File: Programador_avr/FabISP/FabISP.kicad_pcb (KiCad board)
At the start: 2 copper layers, 31.5 x 59.5 mm, 14 parts, among them IC1 ATTINY44-SSU, M1 RESONATOR, M2 PINHD-1x02-SMD-HEADER, M3 MICRO-USB_1_64

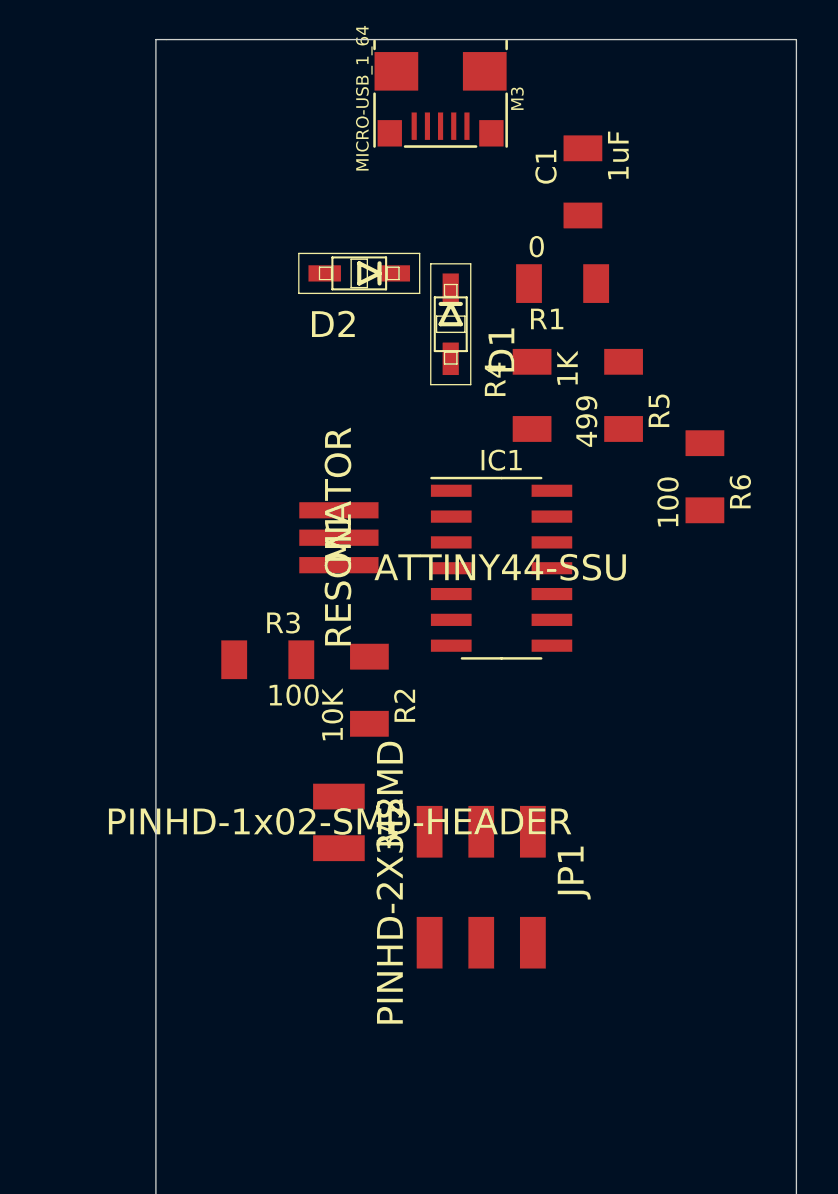
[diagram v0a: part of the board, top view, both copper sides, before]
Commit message: corrección de huellas y primeras rutas de pcb
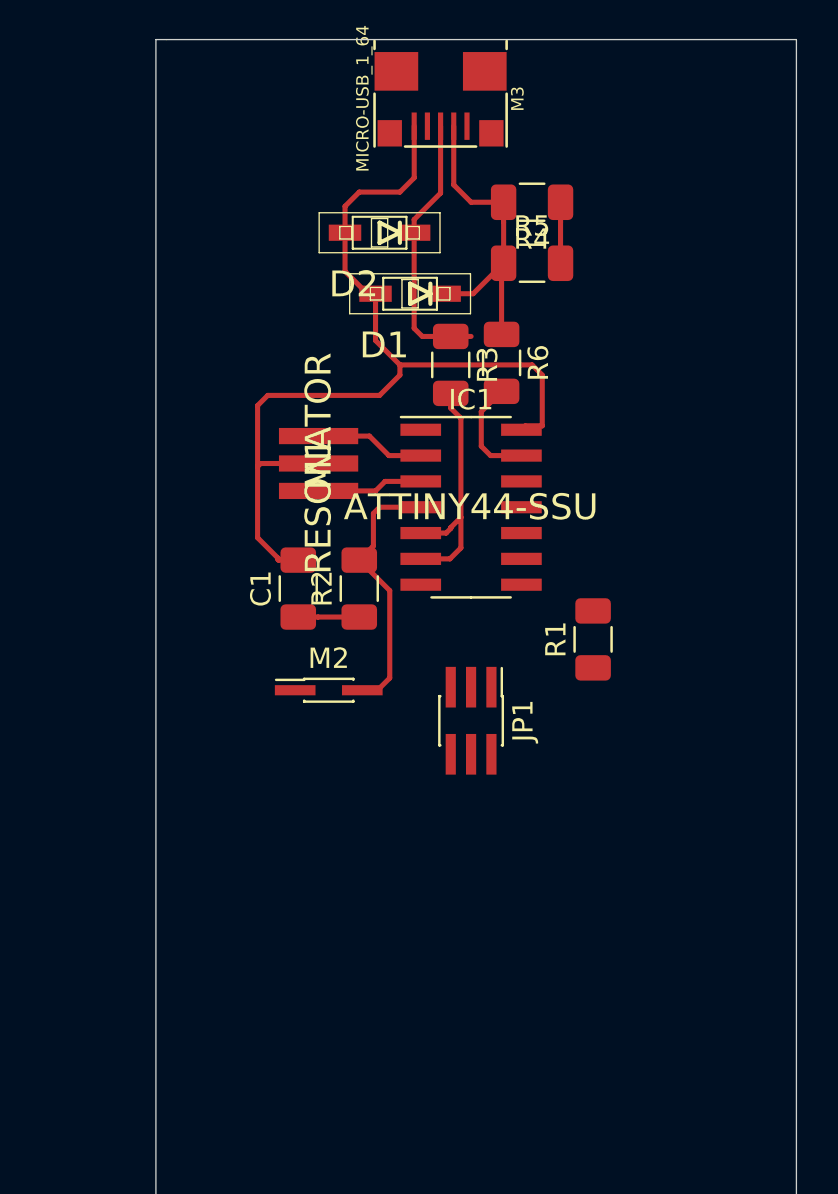
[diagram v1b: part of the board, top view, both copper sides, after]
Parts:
- C1: footprint fab:fab-C1206FAB -> Capacitor_SMD:C_1206_3216Metric
- JP1: footprint fab:fab-2X03SMD -> Connector_PinHeader_1.00mm:PinHeader_2x03_P1.00mm_Vertical_SMD
- M2: footprint fab:fab-1X02SMD -> Connector_PinHeader_1.00mm:PinHeader_2x01_P1.00mm_Vertical_SMD
- R1, R2, R3, R4, R5, R6: footprint fab:fab-R1206FAB -> Resistor_SMD:R_1206_3216Metric
- moved C1 24.4 mm to (91.0, 56.5)
- moved R1 17.6 mm to (105.5, 59.0), turned to 90 degrees
- moved R3 17.1 mm to (98.5, 45.5), turned to 270 degrees
- moved R6 11.5 mm to (101.0, 45.4)
- moved R4 9.50 mm to (102.5, 37.5), turned to 180 degrees
- moved JP1 8.02 mm to (99.5, 63.0)
- moved R5 7.91 mm to (102.5, 40.5), turned to 0 degrees
- moved M2 6.52 mm to (92.5, 61.5), turned to 0 degrees
- moved R2 5.02 mm to (94.0, 56.5), turned to 90 degrees
- moved M1 3.79 mm to (92.0, 50.3)
- moved IC1 3.35 mm to (99.5, 52.5)
- moved D1 2.50 mm to (96.5, 42.0), turned to 180 degrees
- moved D2 2.24 mm to (95.0, 39.0)
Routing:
- net GND: track 0.00 -> 46.7 mm
- net /D-: track 0.00 -> 15.8 mm
- net /D+: track 0.00 -> 13.4 mm
- net /PB3: track 0.00 -> 13.1 mm
- net Net-(IC1-Pad5): track 0.00 -> 12.3 mm
- net /XTAL1: track 0.00 -> 5.42 mm
- net Net-(IC1-Pad13): track 0.00 -> 5.28 mm
- net /XTAL2: track 0.00 -> 5.22 mm
- net VCC: track 0.00 -> 3.00 mm
- net Net-(R4-Pad1): track 0.00 -> 3.00 mm

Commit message: pcb 90%
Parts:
- C1: footprint Capacitor_SMD:C_1206_3216Metric -> fab:fab-C1206FAB
- JP1: footprint Connector_PinHeader_1.00mm:PinHeader_2x03_P1.00mm_Vertical_SMD -> fab:fab-2X03SMD
- M2: footprint Connector_PinHeader_1.00mm:PinHeader_2x01_P1.00mm_Vertical_SMD -> fab:fab-1X02SMD
- R1, R2, R3, R4, R5, R6: footprint Resistor_SMD:R_1206_3216Metric -> fab:fab-R1206FAB
- moved M3 37.5 mm to (74.7, 61.5), turned to 270 degrees
- moved R4 29.8 mm to (80.0, 57.0), turned to 270 degrees
- moved D2 28.9 mm to (81.5, 64.5), turned to 270 degrees
- moved R5 25.5 mm to (83.0, 57.0), turned to 90 degrees
- moved D1 24.2 mm to (84.5, 63.0), turned to 270 degrees
- moved R3 18.7 mm to (88.0, 61.0), turned to 0 degrees
- moved R6 18.5 mm to (87.9, 58.5), turned to 0 degrees
- moved R1 18.0 mm to (88.0, 55.0), turned to 180 degrees
- moved C1 17.7 mm to (104.0, 68.5), turned to 180 degrees
- moved M1 17.2 mm to (93.5, 67.5), turned to 90 degrees
- moved R2 13.8 mm to (104.0, 66.0), turned to 180 degrees
- moved IC1 8.75 mm to (95.0, 60.0), turned to 90 degrees
- moved M2 6.80 mm to (98.0, 65.5), turned to 270 degrees
- moved JP1 6.71 mm to (105.5, 60.0), turned to 0 degrees
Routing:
- net VCC: track 3.00 -> 82.6 mm
- net GND: track 46.7 -> 80.8 mm
- net Net-(JP1-Pad2): track 0.00 -> 20.4 mm
- net /SCK: track 0.00 -> 7.33 mm
- net /XTAL1: track 5.42 -> 9.98 mm
- net /MISO: track 0.00 -> 4.18 mm
- net /D-: track 15.8 -> 19.3 mm
- net /PB3: track 13.1 -> 11.5 mm
- net /XTAL2: track 5.22 -> 3.77 mm
- net /MOSI: track 0.00 -> 1.22 mm
- net /D+: track 13.4 -> 12.5 mm
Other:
- board size 31.5 x 59.5 mm -> 41 x 31.5 mm

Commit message: PCB 100% pendiente para mejoras
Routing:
- net /RST: track 0.00 -> 23.9 mm, vias 0 -> 2
- net /MOSI: track 1.22 -> 10.6 mm
- net Net-(JP1-Pad2): track 20.4 -> 21.4 mm
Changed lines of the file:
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@@
     (thickness 1.6)
     (drawings 7)
-    (tracks 113)
+    (tracks 130)
     (zones 0)
     (modules 14)
@@
   (segment (start 97 60.5) (end 97.54 61.04) (width 0.25) (layer F.Cu) (net 8))
   (segment (start 98.81 62.475) (end 100.025 62.475) (width 0.25) (layer F.Cu) (net 9))
+  (segment (start 100.025 62.475) (end 101.25 61.25) (width 0.25) (layer F.Cu) (net 9))
+  (segment (start 106.89846 60) (end 108.41846 60) (width 0.25) (layer F.Cu) (net 9))
+  (segment (start 105.64846 61.25) (end 106.89846 60) (width 0.25) (layer F.Cu) (net 9))
+  (segment (start 101.25 61.25) (end 105.64846 61.25) (width 0.25) (layer F.Cu) (net 9))
   (segment (start 102.895 57.525) (end 102.96 57.46) (width 0.25) (layer F.Cu) (net 10))
   (segment (start 98.81 57.525) (end 102.895 57.525) (width 0.25) (layer F.Cu) (net 10))
@@
   (segment (start 97.54 59.04) (end 97.54 57.525) (width 0.25) (layer F.Cu) (net 11))
   (segment (start 98 59.5) (end 97.54 59.04) (width 0.25) (layer F.Cu) (net 11))
+  (segment (start 101.595 62.54) (end 102.96 62.54) (width 0.25) (layer F.Cu) (net 12))
+  (segment (start 99.27 64.865) (end 101.595 62.54) (width 0.25) (layer F.Cu) (net 12))
+  (segment (start 99.27 65.5) (end 99.27 64.865) (width 0.25) (layer F.Cu) (net 12))
+  (segment (start 96.27 57.525) (end 96.27 55.73) (width 0.25) (layer F.Cu) (net 12))
+  (via (at 103 55.5) (size 0.8) (drill 0.4) (layers F.Cu B.Cu) (net 12))
+  (segment (start 96.5 55.5) (end 103 55.5) (width 0.25) (layer F.Cu) (net 12))
+  (segment (start 96.27 55.73) (end 96.5 55.5) (width 0.25) (layer F.Cu) (net 12))
+  (via (at 103 64) (size 0.8) (drill 0.4) (layers F.Cu B.Cu) (net 12))
+  (segment (start 103 55.5) (end 103 64) (width 0.25) (layer B.Cu) (net 12))
+  (segment (start 103 62.58) (end 102.96 62.54) (width 0.25) (layer F.Cu) (net 12))
+  (segment (start 103 64) (end 103 62.58) (width 0.25) (layer F.Cu) (net 12))
   (segment (start 92.46 59.04) (end 92.46 57.525) (width 0.25) (layer F.Cu) (net 15) (status 20))
   (segment (start 92 59.5) (end 92.46 59.04) (width 0.25) (layer F.Cu) (net 15))
   (segment (start 90.3 59.5) (end 92 59.5) (width 0.25) (layer F.Cu) (net 15))
   (segment (start 89.3 58.5) (end 90.3 59.5) (width 0.25) (layer F.Cu) (net 15) (status 10))
-  (segment (start 89.651 55) (end 107 55) (width 0.25) (layer F.Cu) (net 16))
-  (segment (start 108.41846 56.41846) (end 108.41846 57.46) (width 0.25) (layer F.Cu) (net 16))
-  (segment (start 107 55) (end 108.41846 56.41846) (width 0.25) (layer F.Cu) (net 16))
+  (segment (start 108.87846 57) (end 108.41846 57.46) (width 0.25) (layer F.Cu) (net 16))
+  (segment (start 109 57) (end 108.87846 57) (width 0.25) (layer F.Cu) (net 16))
+  (segment (start 109 56.5) (end 109 57) (width 0.25) (layer F.Cu) (net 16))
+  (segment (start 107 54.5) (end 109 56.5) (width 0.25) (layer F.Cu) (net 16))
+  (segment (start 89.651 54.5) (end 107 54.5) (width 0.25) (layer F.Cu) (net 16))
   (segment (start 80.975 55.6) (end 83 55.6) (width 0.25) (layer F.Cu) (net 17) (status 20))
   (segment (start 80 55.6) (end 80.975 55.6) (width 0.25) (layer F.Cu) (net 17) (status 10))

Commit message: correcciones sch y pcb
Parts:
- moved M3 27.0 mm to (47.7, 60.2)
- moved R6 27.0 mm to (60.9, 57.2)
- moved C1 27.0 mm to (77.0, 67.2)
- moved D1 27.0 mm to (57.5, 61.8)
- moved D2 27.0 mm to (54.5, 63.2)
- moved IC1 27.0 mm to (68.0, 58.8)
- moved JP1 27.0 mm to (78.5, 58.8)
- moved M1 27.0 mm to (66.5, 66.2)
- moved M2 27.0 mm to (71.0, 64.2)
- moved R1 27.0 mm to (61.0, 53.8)
- moved R2 27.0 mm to (77.0, 64.8)
- moved R3 27.0 mm to (61.0, 59.8)
- moved R4 27.0 mm to (53.0, 55.8)
- moved R5 27.0 mm to (56.0, 55.8)
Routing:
- net /RST: track 23.9 -> 21.8 mm
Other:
- board size 41 x 31.5 mm -> 41 x 19.8 mm

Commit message: correcciones
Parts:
- C1: footprint fab:fab-C1206FAB -> Capacitor_SMD:C_1206_3216Metric
- JP1: footprint fab:fab-2X03SMD -> Connector_PinHeader_1.00mm:PinHeader_2x03_P1.00mm_Vertical_SMD
- M1: value RESONATOR -> Reson.
- M2: footprint fab:fab-1X02SMD -> Connector_PinHeader_1.00mm:PinHeader_2x01_P1.00mm_Vertical_SMD
- R1, R2, R3, R4, R5, R6: footprint fab:fab-R1206FAB -> Resistor_SMD:R_1206_3216Metric
- moved C1 2.02 mm to (79.0, 67.5)
- moved R2 2.02 mm to (79.0, 65.0)
- moved M2 1.77 mm to (71.2, 66.0)
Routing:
- net GND: track 80.8 -> 72.3 mm
- net /PB3: track 11.5 -> 3.79 mm
- net /MOSI: track 10.6 -> 2.95 mm
- net /MISO: track 4.18 -> 6.18 mm
- net /RST: track 21.8 -> 23.1 mm
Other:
- board text added: "ISP"

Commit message: Correcciones
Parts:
- removed R1: 0, Resistor_SMD:R_1206_3216Metric
- added M4: PINHD-1x02-SMD-HEADER, Connector_PinHeader_1.00mm:PinHeader_2x01_P1.00mm_Vertical_SMD, F.Cu at (61.0, 54.0)
- moved M2 1.60 mm to (72.8, 66.0), turned to 0 degrees
- moved M1 1.00 mm to (66.5, 65.2)
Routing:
- net GND: track 72.3 -> 87.7 mm
- net /MOSI: track 2.95 -> 16.2 mm, vias 0 -> 2
- net /PB3: track 3.79 -> 16.6 mm
- net VCC: track 82.3 -> 84.7 mm
- net /RST: track 23.1 -> 25.3 mm
- net /XTAL1: track 9.98 -> 8.88 mm
- net /XTAL2: track 3.77 -> 2.77 mm
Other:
- board size 41 x 19.8 mm -> 41 x 19 mm
- board text added: "ISP_AVR_Programmer"
- board text removed: "ISP"

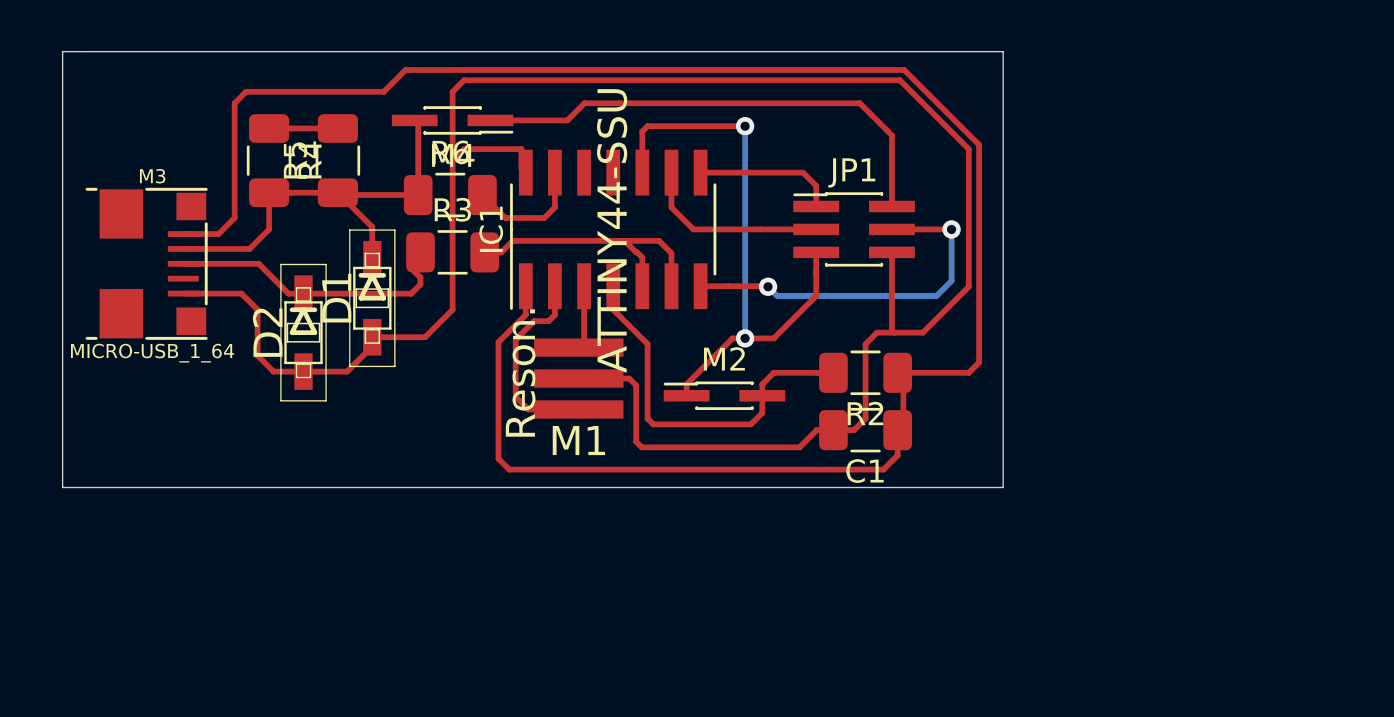
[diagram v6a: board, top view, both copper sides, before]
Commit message: orgnización de serigrafía y correcciones DRC
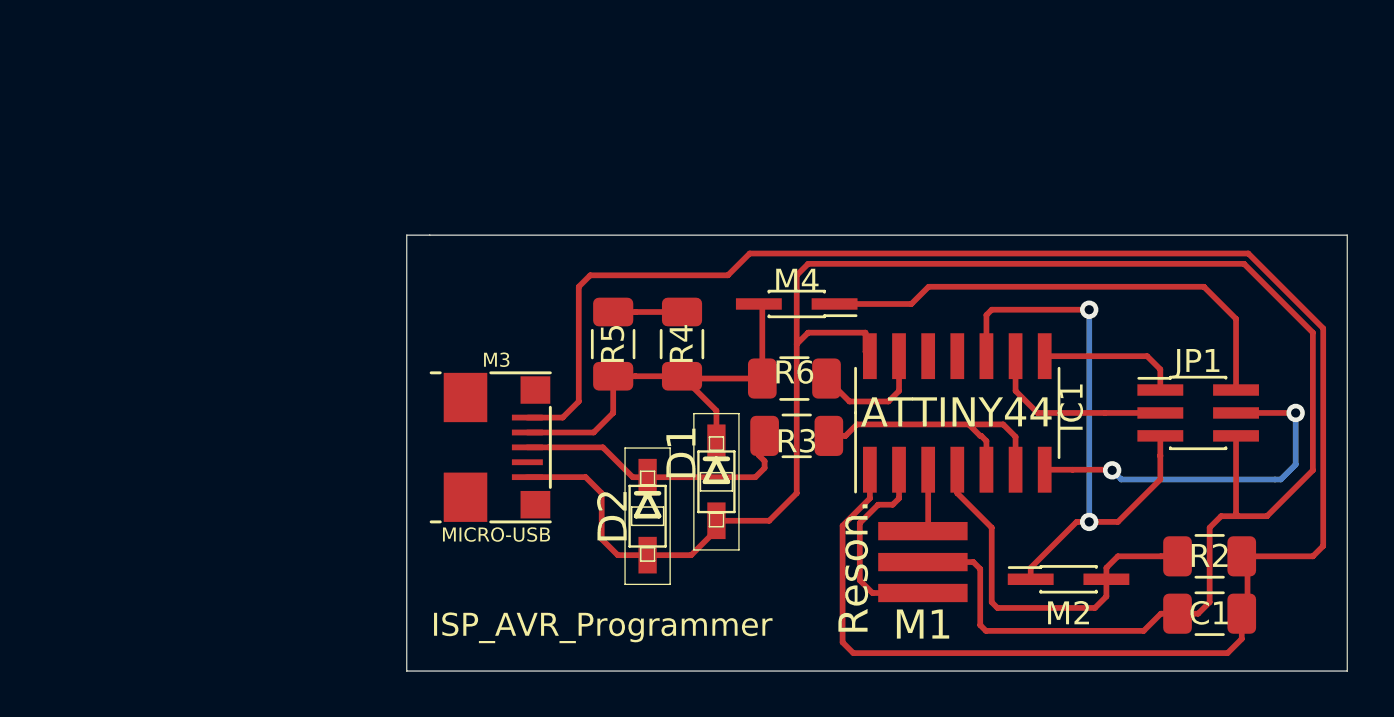
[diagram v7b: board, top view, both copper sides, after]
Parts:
- IC1: value ATTINY44-SSU -> ATTINY44
- M3: value MICRO-USB_1_64 -> MICRO-USB
- moved R6 17.0 mm to (75.9, 65.2)
- moved C1 17.0 mm to (94.0, 75.5)
- moved D1 17.0 mm to (72.5, 69.8)
- moved D2 17.0 mm to (69.5, 71.2)
- moved IC1 17.0 mm to (83.0, 66.8)
- moved JP1 17.0 mm to (93.5, 66.8)
- moved M1 17.0 mm to (81.5, 73.2)
- moved M2 17.0 mm to (87.8, 74.0)
- moved M3 17.0 mm to (62.7, 68.2)
- moved M4 17.0 mm to (76.0, 62.0)
- moved R2 17.0 mm to (94.0, 73.0)
- moved R3 17.0 mm to (76.0, 67.8)
- moved R4 17.0 mm to (68.0, 63.8)
- moved R5 17.0 mm to (71.0, 63.8)

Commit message: Generación de BOM y gerbers
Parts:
- IC1: value ATTINY44 -> ATTINY44-SSU
- M3: value MICRO-USB -> MICRO-USB_1_64
- moved C1 72.3 mm to (160.5, 104.0)
- moved D1 72.3 mm to (139.0, 98.2)
- moved D2 72.3 mm to (136.0, 99.8)
- moved IC1 72.3 mm to (149.5, 95.2)
- moved JP1 72.3 mm to (160.0, 95.2)
- moved M1 72.3 mm to (148.0, 101.8)
- moved M2 72.3 mm to (154.3, 102.5)
- moved M3 72.3 mm to (129.2, 96.8)
- moved M4 72.3 mm to (142.5, 90.5)
- moved R2 72.3 mm to (160.5, 101.5)
- moved R3 72.3 mm to (142.5, 96.2)
- moved R4 72.3 mm to (134.5, 92.2)
- moved R5 72.3 mm to (137.5, 92.2)
- moved R6 72.3 mm to (142.4, 93.8)
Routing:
- net (no net): track 0.00 -> 5.46 mm
- added copper zone on B.Cu, net (none)
- added copper zone on F.Cu, net (none)
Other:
- board text added: "2020"
